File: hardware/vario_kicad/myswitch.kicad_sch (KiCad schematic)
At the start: 4 parts

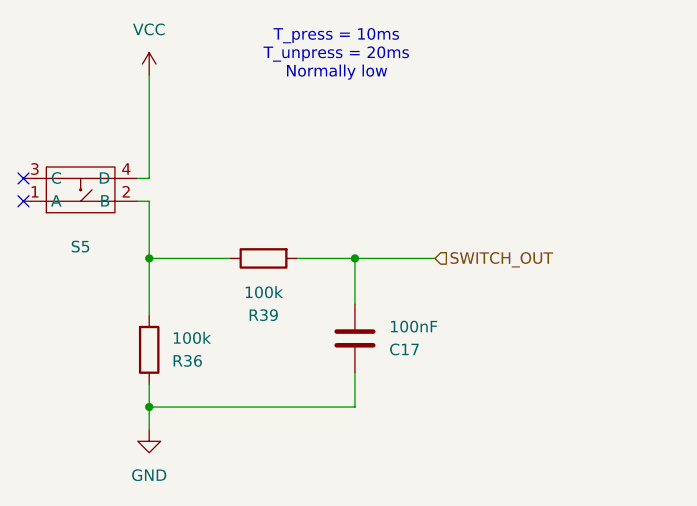
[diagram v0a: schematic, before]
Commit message: add missing footprints
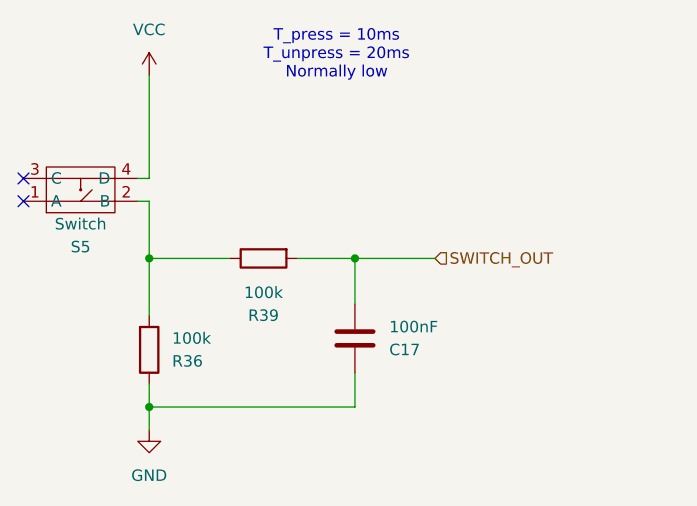
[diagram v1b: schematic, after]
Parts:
- S5: value ~ -> Switch
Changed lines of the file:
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@@
 			)
 		)
-		(property "Value" "~"
+		(property "Value" "Switch"
 			(at 123.19 96.52 0)
 			(effects

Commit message: use 0402 instead of 0603 for almost all caps
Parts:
- C17: footprint Capacitor_SMD:C_0603_1608Metric -> Capacitor_SMD:C_0402_1005Metric
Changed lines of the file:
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@@
 			)
 		)
-		(property "Footprint" "Capacitor_SMD:C_0603_1608Metric"
+		(property "Footprint" "Capacitor_SMD:C_0402_1005Metric"
 			(at 154.6352 105.41 0)
 			(effects

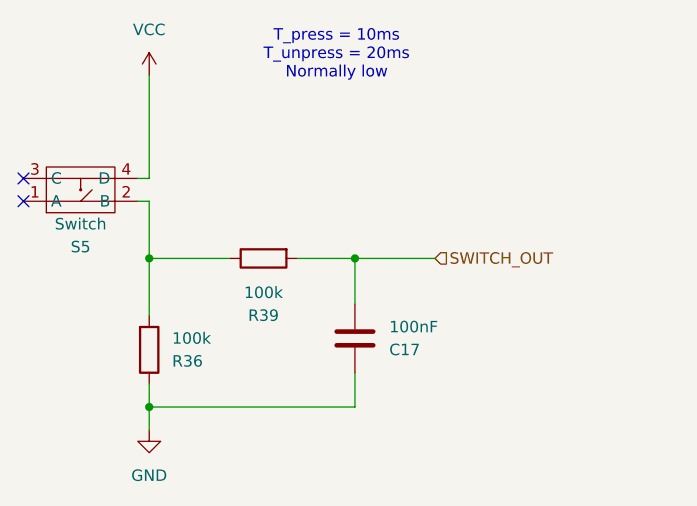
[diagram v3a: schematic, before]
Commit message: fix debounce circuit for wkup1
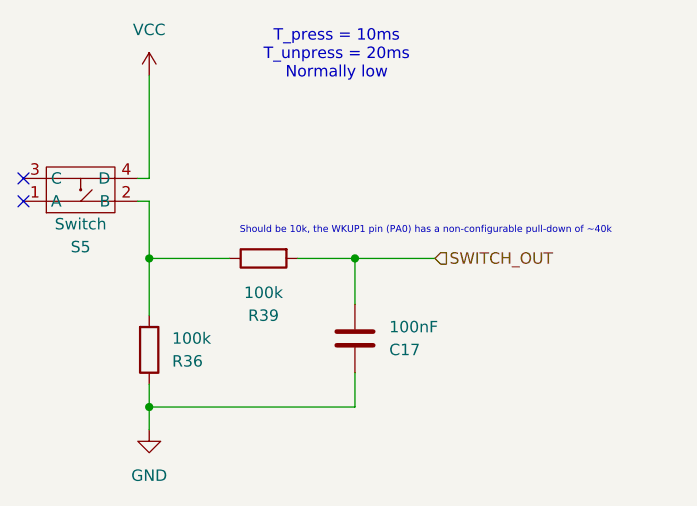
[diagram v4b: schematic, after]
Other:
- note added: "Should be 10k, the WKUP1 pin (PA0) has a non-configurable pull-down of ~40k"
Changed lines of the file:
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@@
+		)
+	)
+	(text "Should be 10k, the WKUP1 pin (PA0) has a non-configurable pull-down of ~40k"
+		(exclude_from_sim no)
+		(at 161.544 97.282 0)
+		(effects
+			(font
+				(size 0.762 0.762)
+			)
 		)
 	)
